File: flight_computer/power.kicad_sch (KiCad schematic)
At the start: 29 parts, among them J3 Conn_01x02, Q2 Q_NMOS_GSD, U2 NCS325, U3 TPS63051RMWR, U4 MIC94310-GYMT-TR

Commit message: Start of layout
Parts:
- C17, C19, C20, C22: footprint Capacitor_SMD:C_0201_0603Metric -> Capacitor_SMD:C_0402_1005Metric
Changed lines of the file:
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@@
       (effects (font (size 1.27 1.27)) (justify left))
     )
-    (property "Footprint" "Capacitor_SMD:C_0201_0603Metric" (at 265.1252 97.79 0)
+    (property "Footprint" "Capacitor_SMD:C_0402_1005Metric" (at 265.1252 97.79 0)
       (effects (font (size 1.27 1.27)) hide)
     )
@@
       (effects (font (size 1.27 1.27)) (justify left))
     )
-    (property "Footprint" "Capacitor_SMD:C_0201_0603Metric" (at 281.6352 97.79 0)
+    (property "Footprint" "Capacitor_SMD:C_0402_1005Metric" (at 281.6352 97.79 0)
       (effects (font (size 1.27 1.27)) hide)
     )
@@
       (effects (font (size 1.27 1.27)) (justify left))
     )
-    (property "Footprint" "Capacitor_SMD:C_0201_0603Metric" (at 314.6552 96.52 0)
+    (property "Footprint" "Capacitor_SMD:C_0402_1005Metric" (at 314.6552 96.52 0)
       (effects (font (size 1.27 1.27)) hide)
     )
@@
       (effects (font (size 1.27 1.27)) (justify left))
     )
-    (property "Footprint" "Capacitor_SMD:C_0201_0603Metric" (at 155.9052 86.36 0)
-      (effects (font (size 1.27 1.27)) hide)
-    )
+    (property "Footprint" "Capacitor_SMD:C_0402_1005Metric" (at 155.9052 86.36 0)
+      (effects (font (size 1.27 1.27)) hide)
+    )

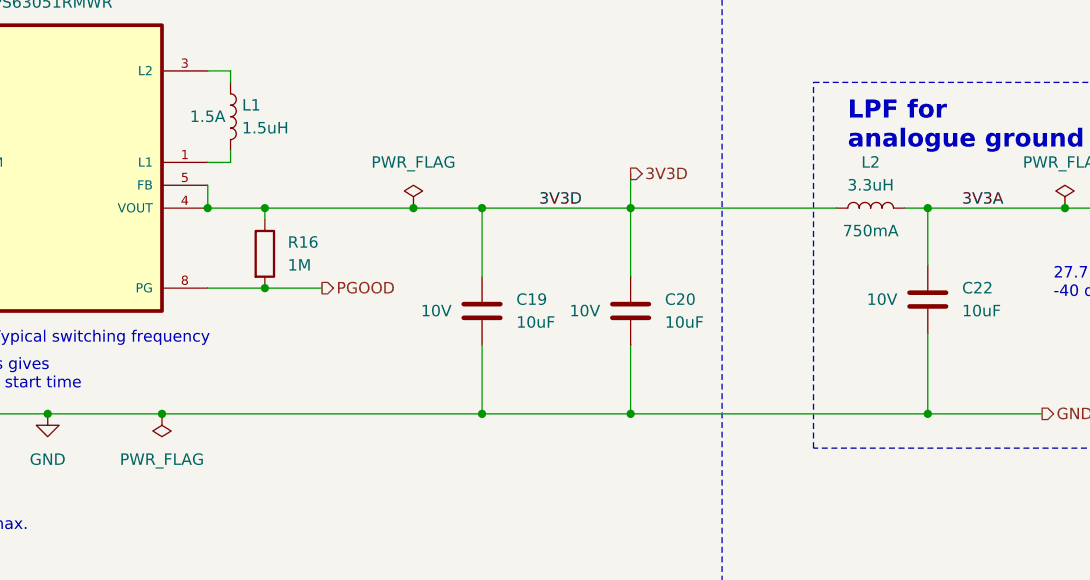
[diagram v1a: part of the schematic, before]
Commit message: finsihed grouping the layout
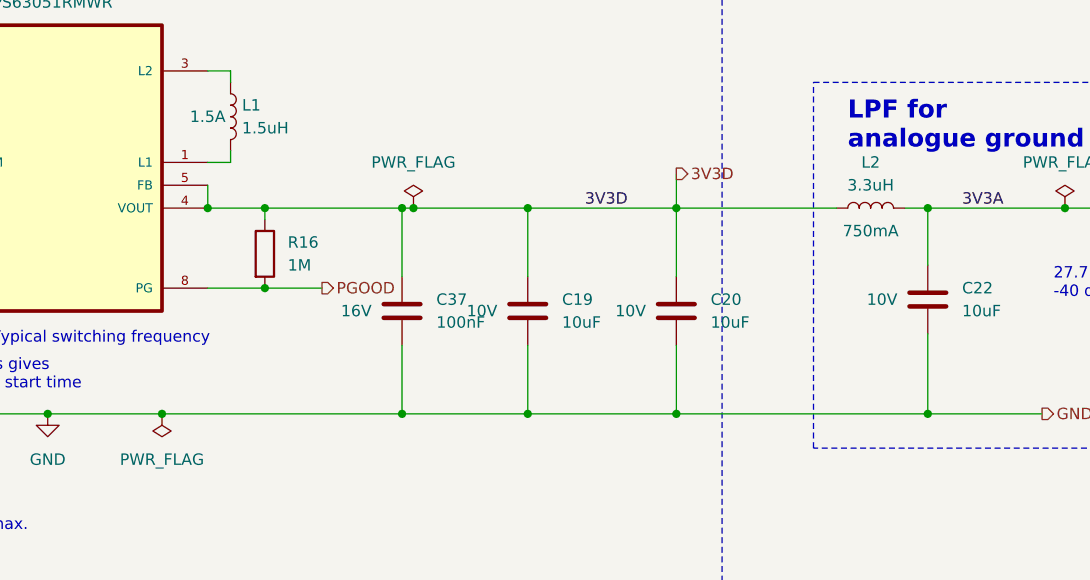
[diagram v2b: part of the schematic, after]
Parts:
- added C37: 100nF, Capacitor_SMD:C_0402_1005Metric, symbol Device:C
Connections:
- net 3V3D: now also C37.1
- net GND: now also C37.2
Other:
- moved on the sheet: C19, C20

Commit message: Most of the way through relayout and new antenna
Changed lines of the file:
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@@
   )
   (symbol (lib_id "Device:C") (at 306.07 190.5 0) (unit 1)
-    (in_bom yes) (on_board yes) (dnp no)
-    (property "Reference" "C6" (at 309.88 189.23 0)
-      (effects (font (size 1.27 1.27)) (justify left))
-    )
-    (property "Value" "1uF" (at 309.88 191.77 0)
+    (in_bom yes) (on_board yes) (dnp no) (fields_autoplaced)
+    (property "Reference" "C6" (at 309.88 187.96 0)
+      (effects (font (size 1.27 1.27)) (justify left))
+    )
+    (property "Value" "1uF" (at 309.88 190.5 0)
       (effects (font (size 1.27 1.27)) (justify left))
     )
@@
       (effects (font (size 1.27 1.27)) hide)
     )
-    (property "Voltage" "25V" (at 300.99 190.5 0)
-      (effects (font (size 1.27 1.27)))
+    (property "Voltage" "25V" (at 309.88 193.04 0)
+      (effects (font (size 1.27 1.27)) (justify left))
     )
     (pin "1")
@@
   )
   (symbol (lib_id "Device:C") (at 359.41 190.5 0) (unit 1)
-    (in_bom yes) (on_board yes) (dnp no)
-    (property "Reference" "C6" (at 363.22 189.23 0)
-      (effects (font (size 1.27 1.27)) (justify left))
-    )
-    (property "Value" "1uF" (at 363.22 191.77 0)
+    (in_bom yes) (on_board yes) (dnp no) (fields_autoplaced)
+    (property "Reference" "C6" (at 363.22 187.96 0)
+      (effects (font (size 1.27 1.27)) (justify left))
+    )
+    (property "Value" "1uF" (at 363.22 190.5 0)
       (effects (font (size 1.27 1.27)) (justify left))
     )
@@
       (effects (font (size 1.27 1.27)) hide)
     )
-    (property "Voltage" "25V" (at 354.33 190.5 0)
-      (effects (font (size 1.27 1.27)))
-    )
-    (pin "1")
+    (property "Voltage" "25V" (at 363.22 193.04 0)
+      (effects (font (size 1.27 1.27)) (justify left))
+    )
+    (pin "1")
